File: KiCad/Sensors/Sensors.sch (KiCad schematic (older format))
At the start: 15 parts, among them J1 Conn_02x06_Odd_Even, U1 OPA1641

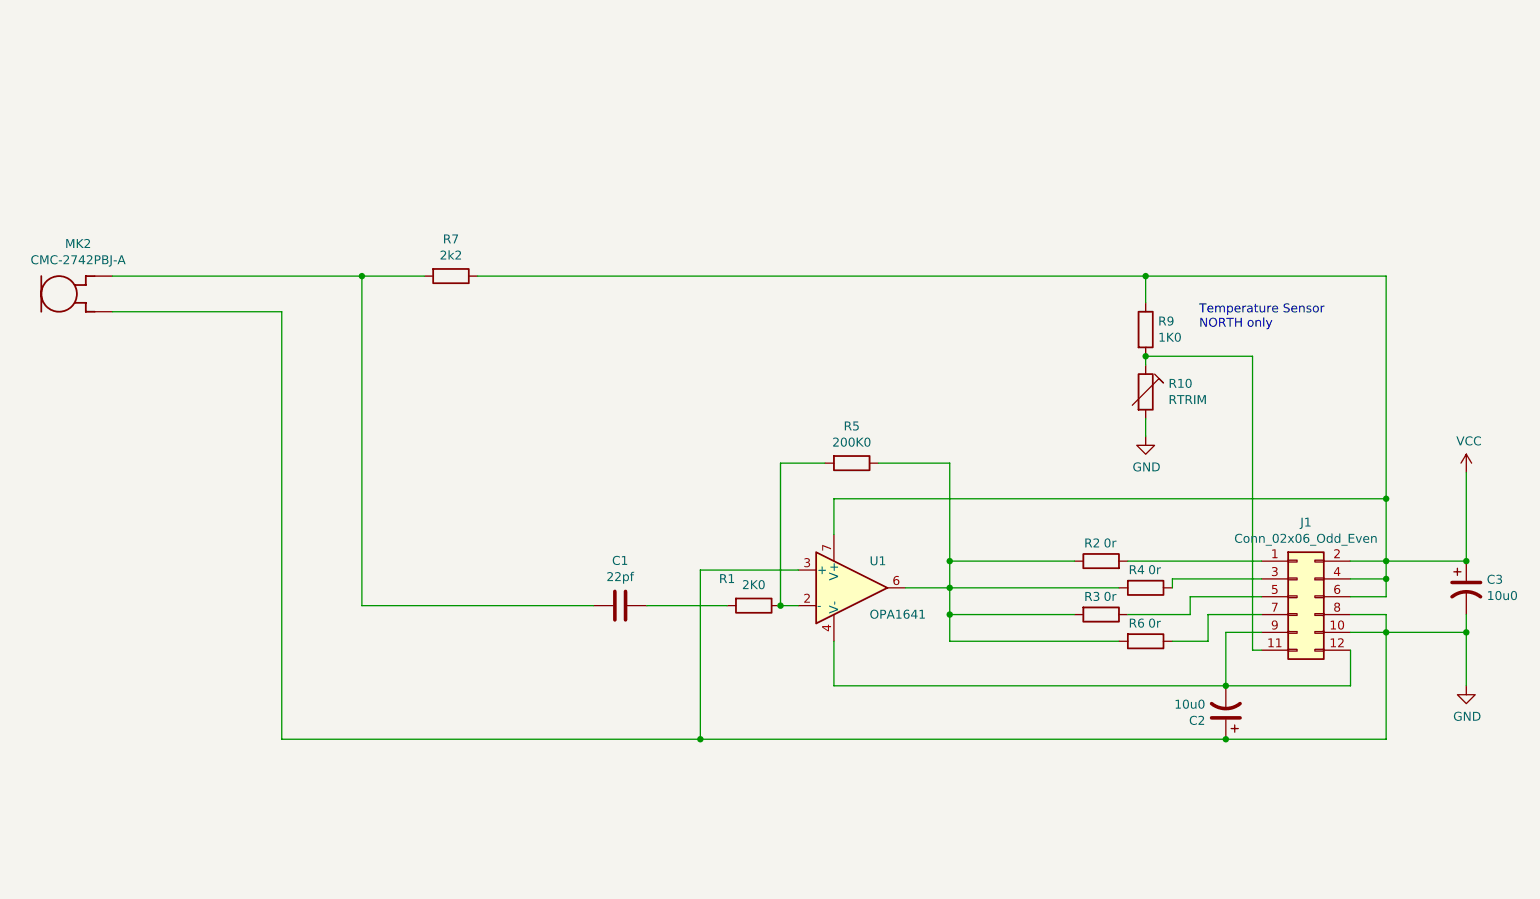
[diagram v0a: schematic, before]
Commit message: Using digital thermometer
Changes to the circuit to support an I2C termometer in place of the RTD
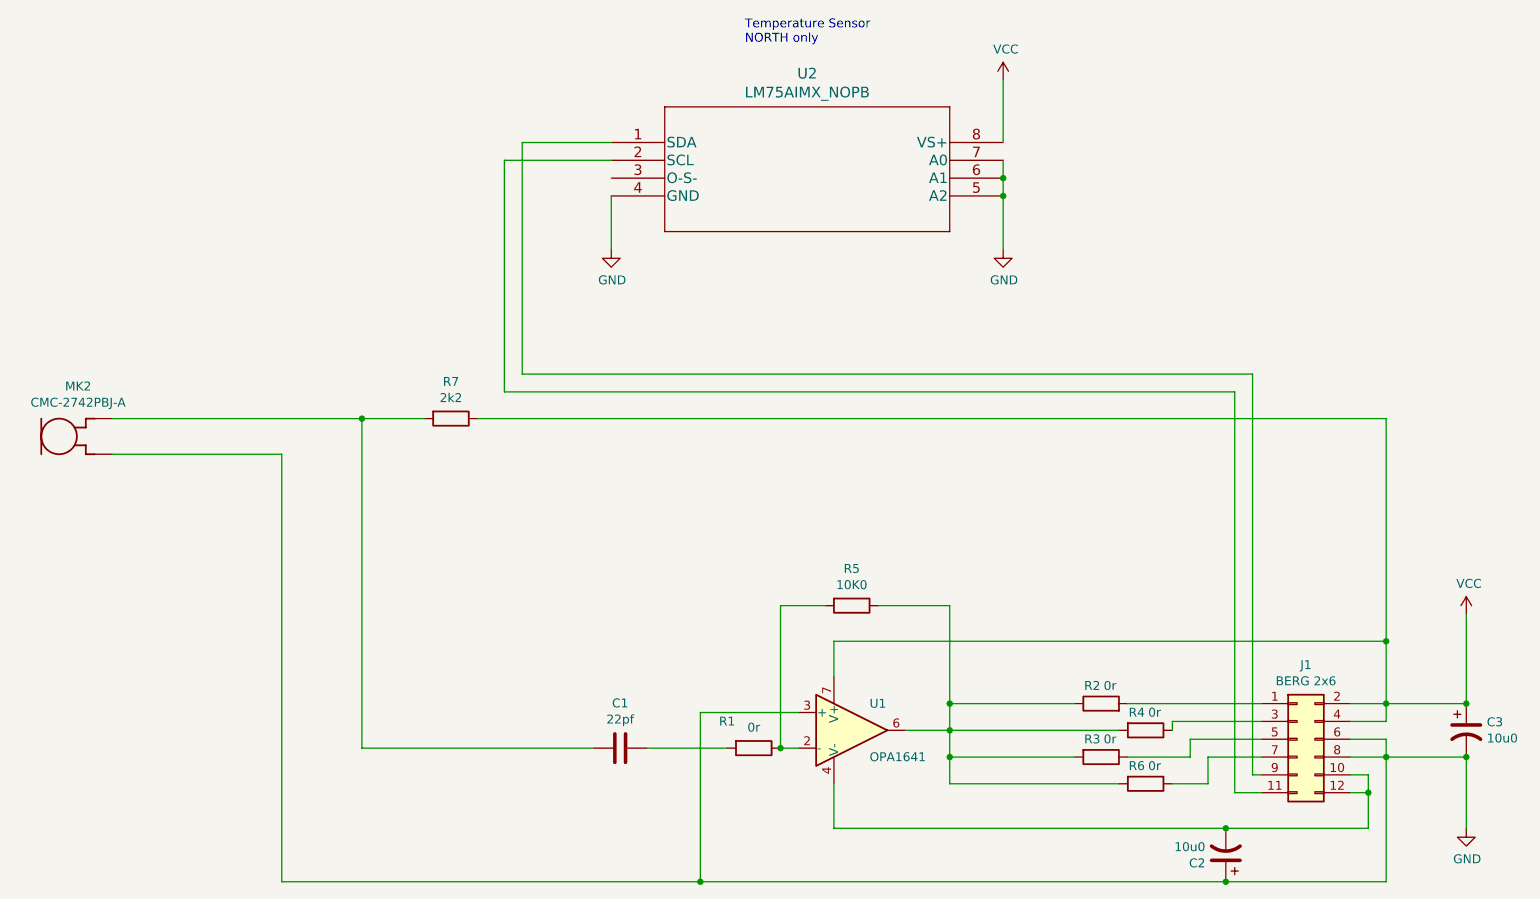
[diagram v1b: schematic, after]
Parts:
- removed R10: RTRIM, Resistor_SMD:R_0805_2012Metric, symbol Device:RTRIM
- removed R9: 1K0, Resistor_SMD:R_0805_2012Metric, symbol Device:R
- added U2: LM75AIMX_NOPB, Package_SO:SOIC-8-1EP_3.9x4.9mm_P1.27mm_EP2.29x3mm, symbol 2020-05-12_18-19-55:LM75AIMX_NOPB
- J1: value Conn_02x06_Odd_Even -> BERG 2x6
- R1: value 2K0 -> 0r
- R5: value 200K0 -> 10K0
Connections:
- net GND: now also J1.6 (Pin_6), U2.4 (GND), U2.5 (A2), U2.6 (A1), U2.7 (A0); no longer J1.10 (Pin_10)
- net VCC: now also U2.8 (VS+); no longer J1.6 (Pin_6)
- net at C2.2, J1.12 (Pin_12), U1.4 (V-): now also J1.10 (Pin_10); no longer J1.9 (Pin_9)
- net at J1.11 (Pin_11): now also U2.2 (SCL)
- new net: J1.9 (Pin_9), U2.1 (SDA)
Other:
- moved on the sheet: C1, C2, C3, J1, MK2, R1, R2, R3, R4, R5, R6, R7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
